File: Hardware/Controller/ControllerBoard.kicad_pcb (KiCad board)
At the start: 2 copper layers, 25 x 140 mm, 53 parts, among them J1 Conn_01x08_MountingPin, J2 USB_C_Receptacle_USB2.0, J3 Conn_01x02_Male, Q1 BC818, Q2 AO3401A, Q3 BC818, Q4 AO3401A, U1 ESP32-S3-WROOM-1, U2 SN65220, U3 TLV62569DBV, U5 MCP73811T-420I-OT, X1 CON_JST_PH_2PIN_MTPH2, X2 CON_JST_PH_2PIN_MTPH2

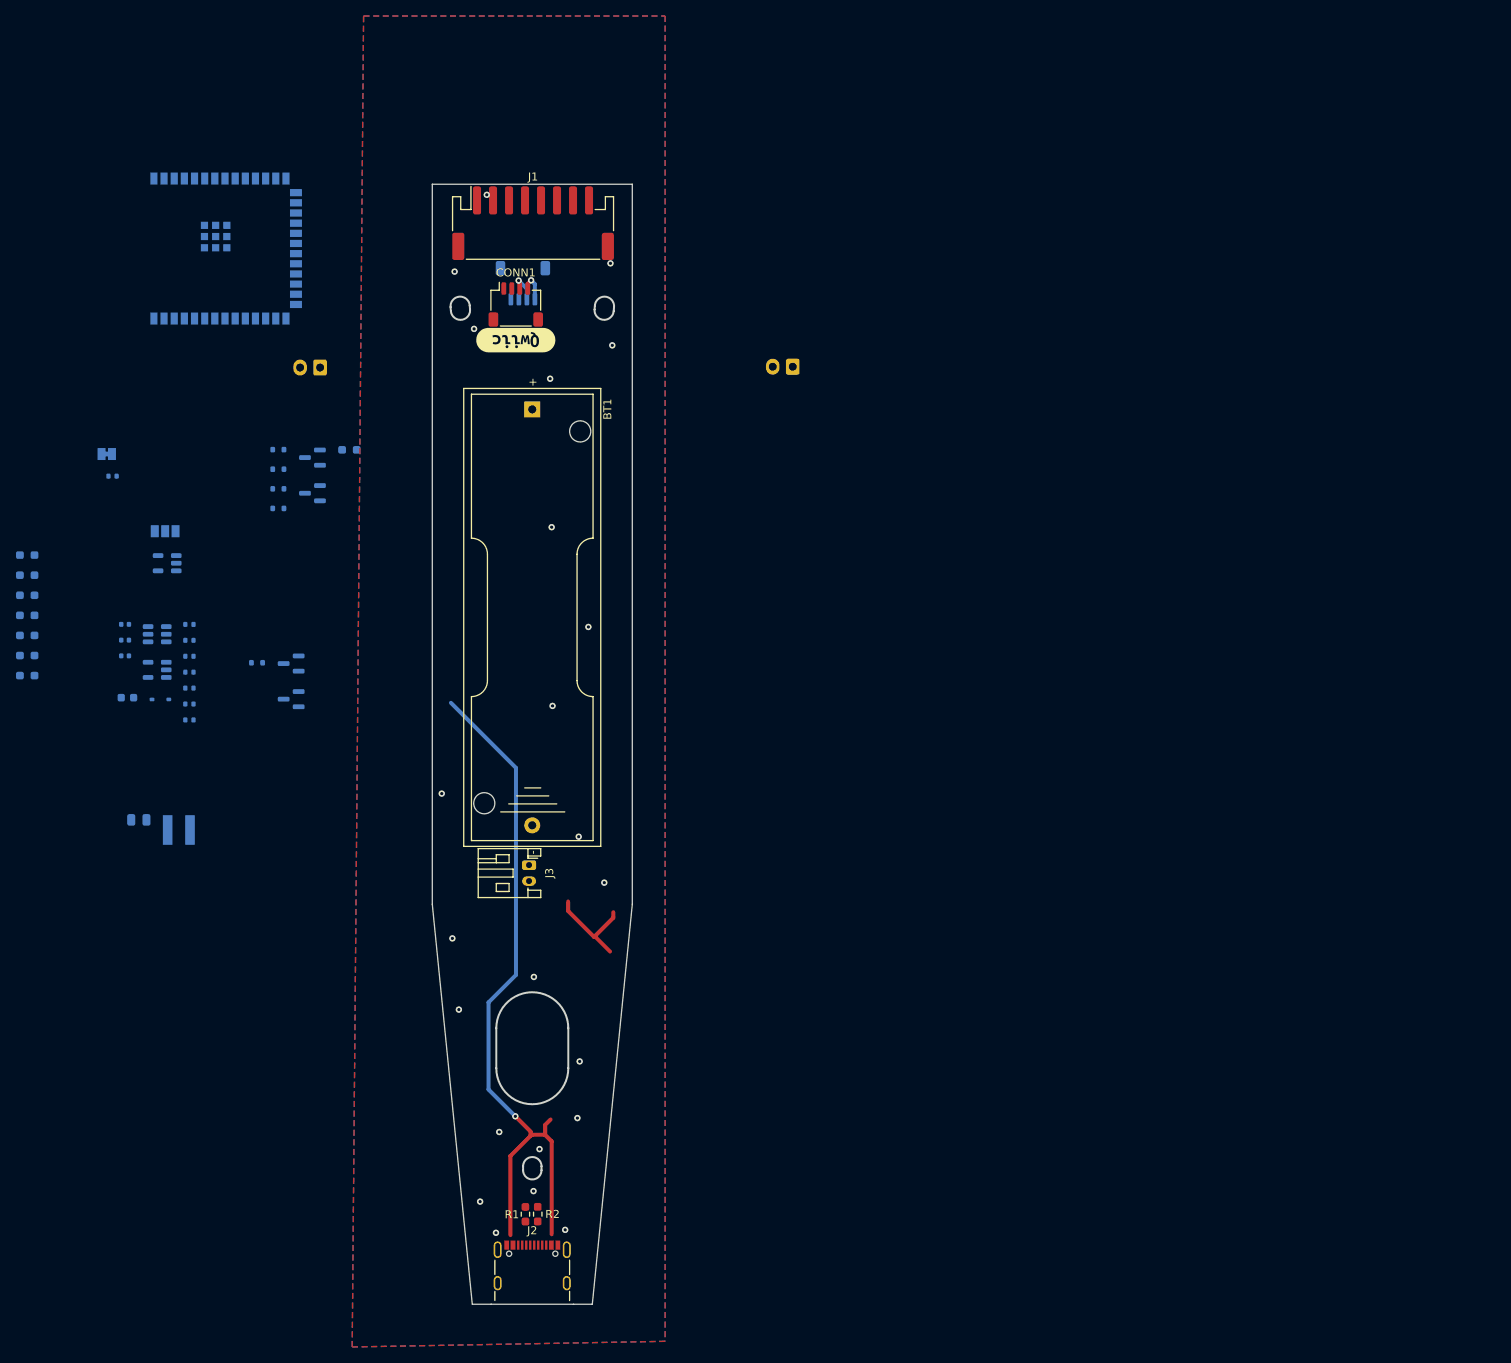
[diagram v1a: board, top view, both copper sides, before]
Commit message: added footprint for MTSM2601SMF1-100
Signed-off-by: lokimetasmith <lokimail@gmail.com>
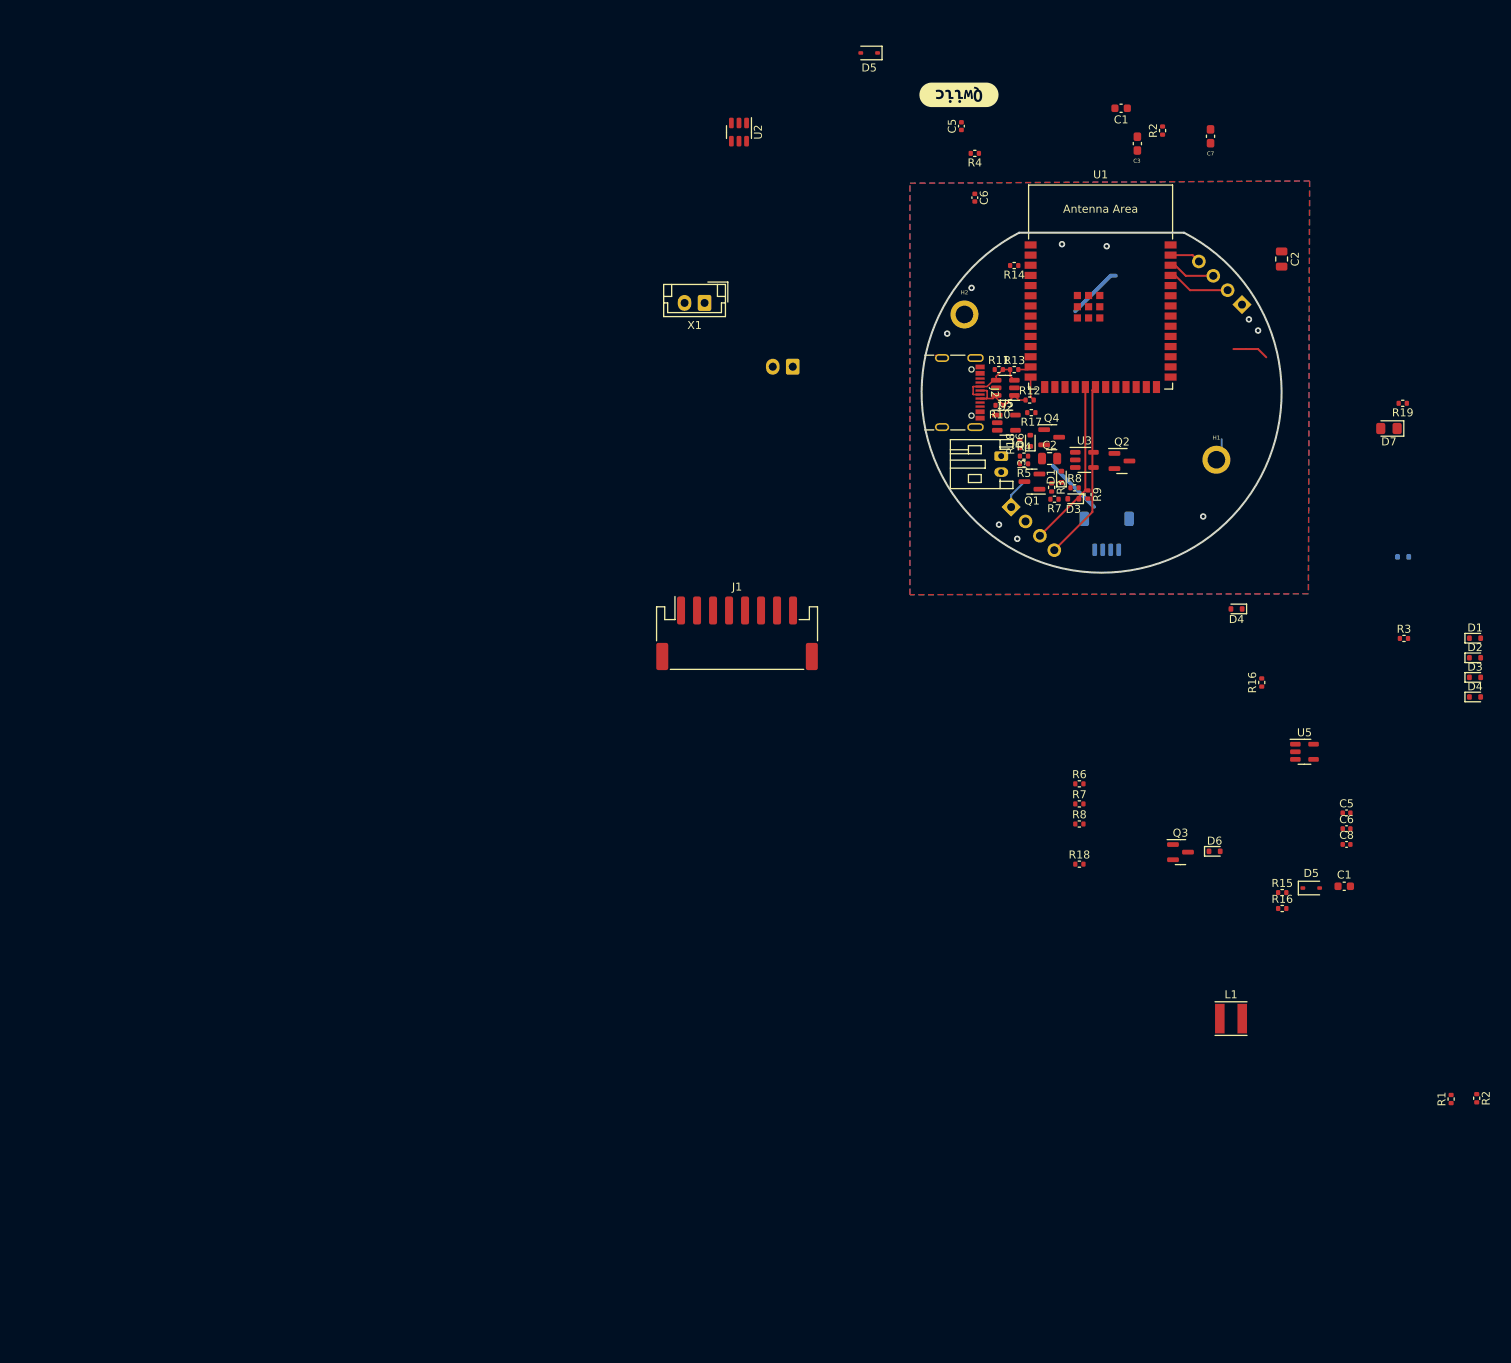
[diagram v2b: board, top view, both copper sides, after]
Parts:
- removed BT1: Battery, Battery:BatteryHolder_Keystone_2460_1xAA
- removed CONN1, CONN2: STEMMA_I2C_QT, Connector_JST:JST_SH_SM04B-SRSS-TB_1x04-1MP_P1.00mm_Horizontal
- removed JP1: SolderJumper_3_Open, Jumper:SolderJumper-3_P1.3mm_Open_Pad1.0x1.5mm_NumberLabels
- removed JP2: SolderJumper_2_Bridged, Jumper:SolderJumper-2_P1.3mm_Bridged_Pad1.0x1.5mm
- removed X2: CON_JST_PH_2PIN_MTPH2, Connector_JST:JST_EH_B2B-EH-A_1x02_P2.50mm_Vertical
- added C1: 2u, Capacitor_SMD:C_0603_1608Metric, F.Cu at (184.3, 25.5)
- added C2: 4.7u, Capacitor_SMD:C_0805_2012Metric, F.Cu at (204.3, 44.3)
- added C3: 51pF, Capacitor_SMD:C_0603_1608Metric_Pad1.08x0.95mm_HandSolder, F.Cu at (186.3, 29.9)
- added C5: 6.8p, Capacitor_SMD:C_0402_1005Metric, F.Cu at (164.3, 27.7)
- added C6: 0.01u, Capacitor_SMD:C_0402_1005Metric, F.Cu at (166.0, 36.7)
- added C7: 0.1uF, Capacitor_SMD:C_0603_1608Metric_Pad1.08x0.95mm_HandSolder, F.Cu at (195.4, 29.0)
- added D1: BAS516, Diode_SMD:D_SOD-523, F.Cu at (176.8, 71.6)
- added D2: BAS516, Diode_SMD:D_SOD-523, B.Cu at (219.5, 81.6)
- added D3: BAS516, Diode_SMD:D_SOD-523, F.Cu at (178.3, 74.3)
- added D4: BAS516, Diode_SMD:D_SOD-523, F.Cu at (198.7, 88.1)
- added D5: 3.3v_TVS, Diode_SMD:D_SOD-323, F.Cu at (152.8, 18.6)
- added D6: BAS516, Diode_SMD:D_SOD-523, F.Cu at (172.9, 67.1)
- added D7: POWER LED, LED_SMD:LED_0805_2012Metric_Pad1.15x1.40mm_HandSolder, F.Cu at (217.7, 65.5)
- added H1: MountingHole, MountingHole:MountingHole_2.2mm_M2_ISO7380_Pad, F.Cu at (196.2, 69.4)
- added H2: MountingHole, MountingHole:MountingHole_2.2mm_M2_ISO7380_Pad, F.Cu at (164.7, 51.3)
- added J4: Interface, Connector_PinSocket_2.54mm:PinSocket_1x04_P2.54mm_Vertical, B.Cu at (199.4, 50.0)
- added J5: I2C, Connector_JST:JST_SH_SM04B-SRSS-TB_1x04-1MP_P1.00mm_Horizontal, B.Cu at (182.4, 78.7)
- added J6: I2C ThroughHole, Connector_PinSocket_2.54mm:PinSocket_1x04_P2.54mm_Vertical, B.Cu at (170.5, 75.3)
- added LOGO1: OSHW-Logo_11.4x12mm_SilkScreen, Symbol:OSHW-Logo_11.4x12mm_SilkScreen, B.Cu at (225.1, 41.2)
- added LOGO2: PlasticScannerLogo, PlasticScannerLibrary:PlasticScannerLogo, B.Cu at (228.7, 27.8)
- added R16: 150K, Resistor_SMD:R_0402_1005Metric, F.Cu at (201.8, 97.3)
- added R18: 100k, Resistor_SMD:R_0402_1005Metric, F.Cu at (171.6, 67.5)
- added R19: 150, Resistor_SMD:R_0402_1005Metric, F.Cu at (219.5, 62.4)
- added R2: 5.1k, Resistor_SMD:R_0402_1005Metric, F.Cu at (189.4, 28.3)
- added R3: 1k, Resistor_SMD:R_0402_1005Metric, F.Cu at (175.6, 72.9)
- added R4: 100k, Resistor_SMD:R_0402_1005Metric, F.Cu at (166.0, 31.1)
- added R7: 10k, Resistor_SMD:R_0402_1005Metric, F.Cu at (175.9, 74.4)
- added R8: 100k, Resistor_SMD:R_0402_1005Metric, F.Cu at (178.4, 72.9)
- added U2: SN65220, Package_TO_SOT_SMD:SOT-23-6, F.Cu at (136.5, 28.5)
- added U5: MCP73811T-420I-OT, Package_TO_SOT_SMD:SOT-23-5, F.Cu at (169.9, 64.8)
- added X1: CON_JST_PH_2PIN_MTPH2, Connector_JST:JST_EH_B2B-EH-A_1x02_P2.50mm_Vertical, F.Cu at (132.2, 49.8)
- added kibuzzard-6346913B: G***, PlasticScannerLibrary:kibuzzard-6346913B, B.Cu at (208.3, 29.2)
- added kibuzzard-6398DD41: G***, kibuzzard-6398DD41, B.Cu at (226.3, 56.8)
- C1, C2, C5, C6, C8, D1, D2, D3, D4, D5, D6, L1, Q1, Q2, Q3, Q4, R10, R11, R12, R13, R14, R15, R16, R17, U1, U2, U3, U5: moved to F.Cu
- R1, R2: footprint Resistor_SMD:R_0603_1608Metric_Pad0.98x0.95mm_HandSolder -> Resistor_SMD:R_0402_1005Metric
- R18, R3, R4, R5, R6, R7, R8, R9: footprint Resistor_SMD:R_0603_1608Metric_Pad0.98x0.95mm_HandSolder -> Resistor_SMD:R_0402_1005Metric; moved to F.Cu
- moved C5 154.5 mm to (212.4, 113.6), turned to 0 degrees
- moved C6 154.5 mm to (212.4, 115.6), turned to 0 degrees
- moved C8 154.5 mm to (212.4, 117.5), turned to 0 degrees
- moved C1 153.9 mm to (212.1, 122.8), turned to 0 degrees
- moved D1 151.4 mm to (228.5, 91.7), turned to 0 degrees
- moved D2 151.4 mm to (228.5, 94.2), turned to 0 degrees
- moved D3 151.4 mm to (228.5, 96.6), turned to 0 degrees
- moved D4 151.4 mm to (228.5, 99.1), turned to 0 degrees
- moved D5 145.8 mm to (208.0, 123.0), turned to 0 degrees
- moved U5 144.1 mm to (207.2, 105.9), turned to 0 degrees
- moved R15 138.6 mm to (204.4, 123.5), turned to 0 degrees
- moved R16 138.6 mm to (204.4, 125.5), turned to 0 degrees
- moved R9 134.1 mm to (180.1, 73.8), turned to -90 degrees
- moved R3 133.9 mm to (219.6, 91.8), turned to 0 degrees
- moved L1 133.6 mm to (198.0, 139.3), turned to 0 degrees
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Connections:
- D1 pad 2: Net-(D1-A) -> /Trigger
- D2 pad 1: Net-(D2-K) -> Net-(D1-K)
- Q3 pad 2: unconnected-(Q3-E-Pad2) -> GND
- R18 pad 1: unconnected-(R18-Pad1) -> GND
- U1 pad 19: unconnected-(U1-GPIO11/TOUCH11/ADC2_CH0/FSPID/FSPIIO5/SUBSPID-Pad19) -> SDA
- U1 pad 20: unconnected-(U1-GPIO12/TOUCH12/ADC2_CH1/FSPICLK/FSPIIO6/SUBSPICLK-Pad20) -> SCL
- U1 pad 37: unconnected-(U1-U0TXD/GPIO43/CLK_OUT1-Pad37) -> LED RESET
- U1 pad 38: /Trigger -> AS7341_INT
- U1 pad 39: /KeepAlive -> DRDY_INT
- X1 pad 1: Net-(JP1-C) -> /Trigger
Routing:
- net GND: track 104.0 -> 23.6 mm, vias 24 -> 9
- net +3V3: track 0.00 -> 34.1 mm
- net SCL: track 0.00 -> 22.6 mm
- net SDA: track 0.00 -> 20.9 mm
- net /D+: track 0.00 -> 9.97 mm
- net /D-: track 0.00 -> 9.19 mm
- net LED RESET: track 0.00 -> 7.89 mm
- net AS7341_INT: track 0.00 -> 5.88 mm
- net DRDY_INT: track 0.00 -> 3.87 mm
- net /SCL: track 3.14 -> 0.00 mm, vias 1 -> 0
- net /USB_D+: track 0.00 -> 3.04 mm
- net /SDA: track 2.96 -> 0.00 mm, vias 1 -> 0
- net /USB_D-: track 0.00 -> 1.67 mm
- net /Shield: track 0.00 -> 1.27 mm
- added copper zone on In2.Cu, net +3V3
- added copper zone on In1.Cu, net GND
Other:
- board size 25 x 140 mm -> 45 x 42.5 mm
- copper layers 2 -> 4
- board text added: "3.3v"
- board text added: "AS Int"
- board text added: "DRDY"
- board text added: "Gnd"
- board text added: "HandheldScanner v1.0 2022-12-23"
- board text added: "LEDreset"
- board text added: "Power"
- board text added: "SCL"
- board text added: "SDA"

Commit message: second pass on controller rework
Signed-off-by: lokimetasmith <lokimail@gmail.com>
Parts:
- removed the C1 at (184.3, 25.5)
- removed the C2 at (175.3, 69.3)
- removed the C5 at (212.4, 113.6)
- removed the C6 at (166.0, 36.7)
- removed the D1 at (176.8, 71.6)
- removed the D2 at (219.5, 81.6)
- removed the D3 at (228.5, 96.6)
- removed the D4 at (198.7, 88.1)
- removed the D5 at (152.8, 18.6)
- removed the D6 at (172.9, 67.1)
- removed the R16 at (204.4, 125.5)
- removed the R2 at (189.4, 28.3)
- removed the R3 at (175.6, 72.9)
- removed the R4 at (166.0, 31.1)
- removed the R7 at (179.0, 112.5)
- removed the R8 at (178.4, 72.9)
- removed the U2 at (136.5, 28.5)
- removed the U5 at (207.2, 105.9)
- D7, J1, J3: moved to B.Cu
- J5: moved to F.Cu
- moved R2 110.4 mm to (163.8, 60.0)
- moved R1 106.9 mm to (163.6, 62.2)
- moved C1 89.7 mm to (170.0, 43.6)
- moved C8 82.0 mm to (169.6, 47.6), turned to 90 degrees
- moved C6 81.1 mm to (168.2, 47.6), turned to 90 degrees
- moved L1 75.2 mm to (188.0, 64.8), turned to -90 degrees
- moved D2 74.1 mm to (155.1, 103.8), turned to 90 degrees
- moved X1 69.0 mm to (159.6, 113.2)
- moved D1 68.7 mm to (161.6, 107.4), turned to -90 degrees
- moved D5 66.3 mm to (179.8, 63.0)
- moved J1 63.0 mm to (181.7, 47.5), turned to 180 degrees
- moved D4 62.4 mm to (166.2, 101.3)
- moved R3 59.3 mm to (161.2, 102.3), turned to 90 degrees
- moved R15 57.7 mm to (188.0, 68.2), turned to -90 degrees
- moved R19 54.2 mm to (168.0, 45.4)
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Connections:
- J2 pad A1: Net-(J2-GND-PadA1) -> GND
- J2 pad A12: Net-(J2-GND-PadA1) -> GND
- J2 pad B1: Net-(J2-GND-PadA1) -> GND
- J2 pad B12: Net-(J2-GND-PadA1) -> GND
- U1 pad 23: unconnected-(U1-GPIO21-Pad23) -> /KeepAlive
- U1 pad 26: unconnected-(U1-GPIO45-Pad26) -> /Trigger
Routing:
- net /Trigger_Wake_Up/VBAT: track 0.00 -> 30.5 mm
- net +3V3: track 34.1 -> 7.10 mm
- net SCL: track 22.6 -> 0.00 mm
- net SDA: track 20.9 -> 0.00 mm
- net USB_pwr: track 0.00 -> 15.8 mm
- net GND: track 23.6 -> 10.5 mm, vias 9 -> 4
- net Net-(D1-K): track 0.00 -> 10.8 mm
- net /Trigger: track 0.00 -> 5.93 mm
- net Net-(JP3-B): track 0.00 -> 5.84 mm
- net Net-(D3-K): track 0.00 -> 4.68 mm
- net Net-(Q1-E): track 0.00 -> 3.44 mm
- net Net-(Q1-C): track 0.00 -> 3.26 mm
- net Net-(Q2-G): track 0.00 -> 2.17 mm
- net Net-(U3-FB): track 0.00 -> 2.09 mm
- net Net-(D3-A): track 0.00 -> 1.88 mm
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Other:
- board text removed: "HandheldScanner v1.0 2022-12-23"
